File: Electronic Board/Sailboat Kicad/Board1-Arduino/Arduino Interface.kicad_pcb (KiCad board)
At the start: 2 copper layers, 68.6 x 99.7 mm, 60 parts, among them J1 Conn_01x02, J10 Conn_01x02, J11 Conn_01x03_Male, J12 Conn_01x03_Male, J13 Conn_01x03_Male, J14 Conn_01x03_Male, J15 Conn_01x04, J16 Conn_01x04, J17 Conn_01x04, J18 Conn_01x04, J19 Conn_01x03, J2 Conn_01x08, J20 Conn_01x03, J21 Conn_01x02, J22 Conn_01x02, J23 Conn_01x06, J24 Conn_01x03, J25 Conn_01x06, J26 Conn_02x02_Odd_Even, J27 Conn_01x08, J3 Conn_01x08, J31 Conn_01x04, J32 Conn_01x04, J34 Conn_01x02, J35 Conn_01x02, J36 Conn_01x02, J37 Conn_01x02, J4 Conn_01x08, J5 Conn_02x18_Odd_Even, J6 Conn_01x08, J7 Conn_01x08, J8 Conn_01x08, J9 Conn_01x02, U1 L7805, U2 L7805, U3 L7805

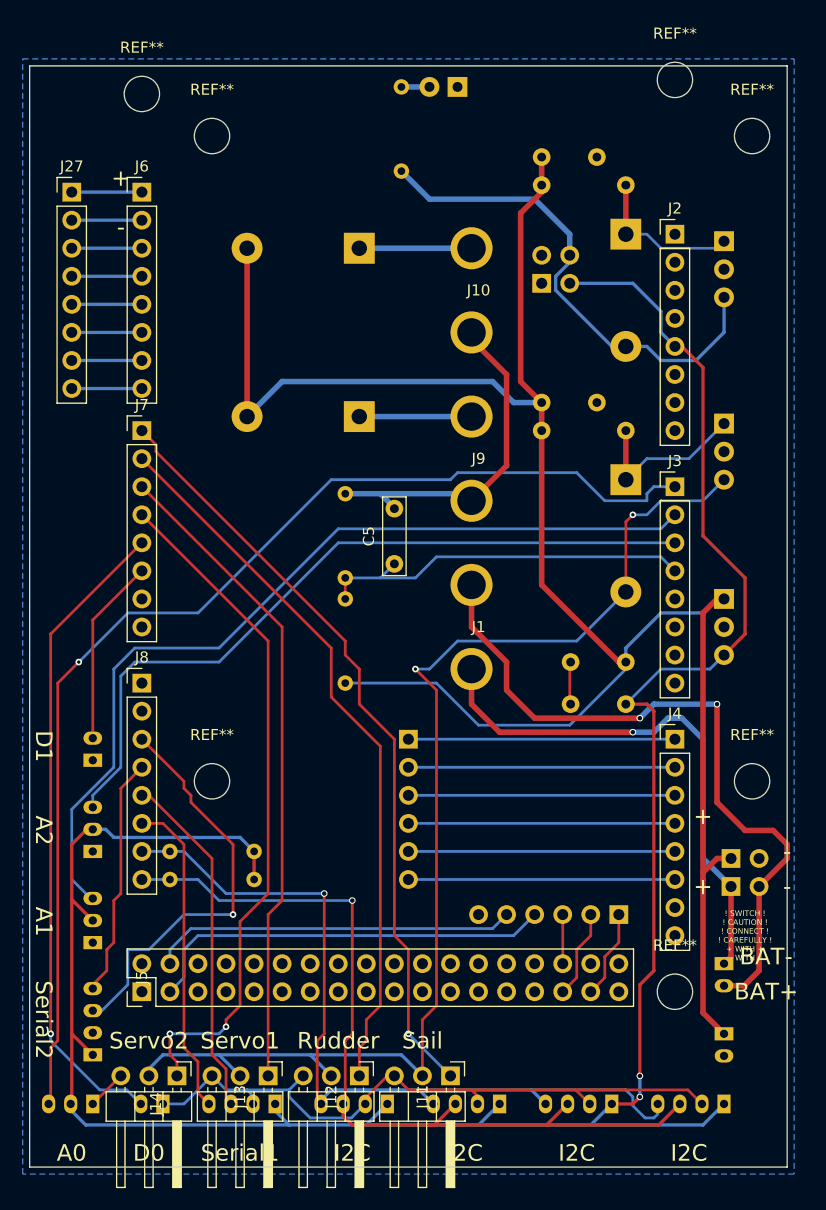
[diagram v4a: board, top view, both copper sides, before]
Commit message: Updated version of Kicad, rendered images and BOM
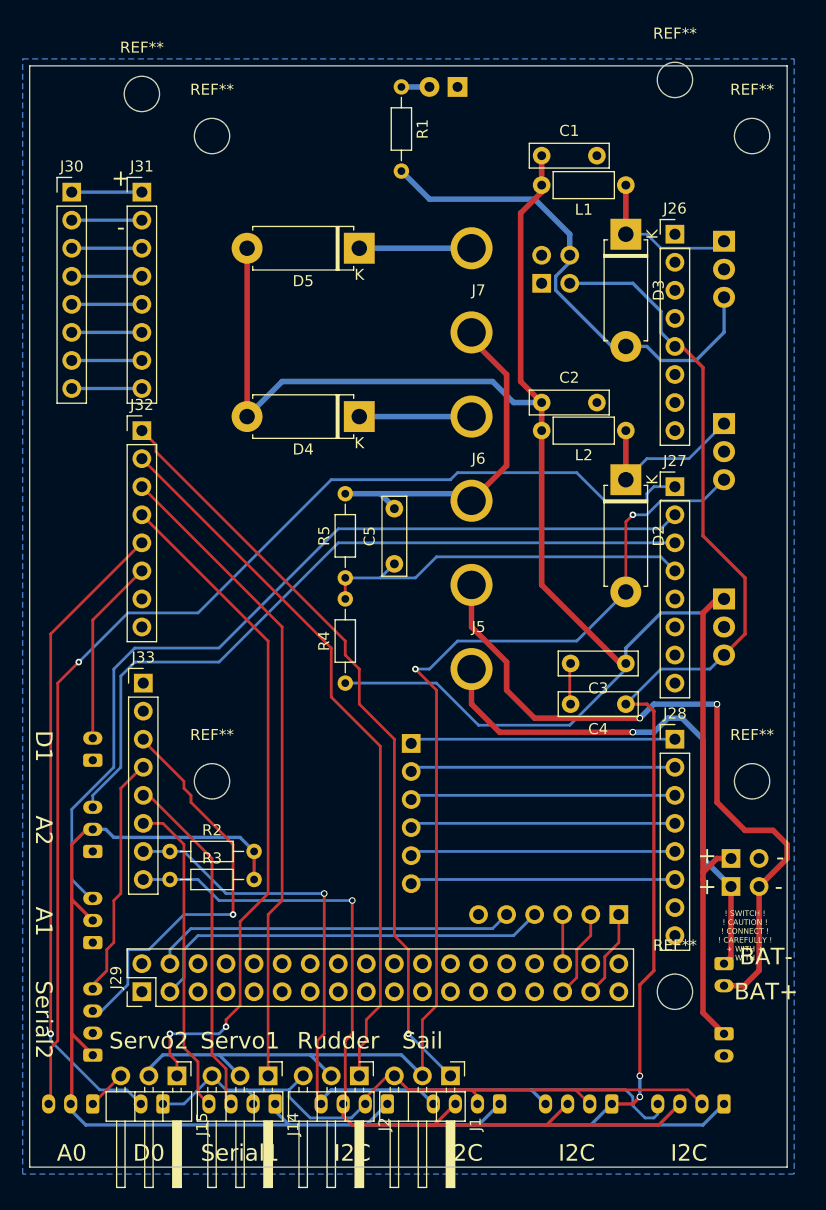
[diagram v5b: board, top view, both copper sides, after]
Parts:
- removed J34, J35: Conn_01x02, Connectors_JST:JST_PH_S2B-PH-K_02x2.00mm_Angled
- removed J36, J37: Conn_01x02, Pin_Headers:Pin_Header_Straight_1x02_Pitch2.54mm
- added J28: Conn_01x08_Male, Connector_PinHeader_2.54mm:PinHeader_1x08_P2.54mm_Vertical, F.Cu at (177.2, 114.3)
- added J29: Conn_02x18_Odd_Even, Connector_PinHeader_2.54mm:PinHeader_2x18_P2.54mm_Vertical, F.Cu at (128.9, 137.2)
- added J30: Conn_01x08_Male, Connector_PinHeader_2.54mm:PinHeader_1x08_P2.54mm_Vertical, F.Cu at (122.6, 64.8)
- added J33: Conn_01x08_Male, Connector_PinHeader_2.54mm:PinHeader_1x08_P2.54mm_Vertical, F.Cu at (129.0, 109.2)
- C1, C2: footprint Capacitors_THT:C_Rect_L7.0mm_W2.0mm_P5.00mm -> Capacitor_THT:C_Rect_L7.0mm_W2.0mm_P5.00mm; moved to F.Cu
- C3, C4: footprint Capacitors_THT:C_Rect_L7.0mm_W3.5mm_P5.00mm -> Capacitor_THT:C_Rect_L7.0mm_W2.0mm_P5.00mm; moved to F.Cu
- C5: footprint Capacitors_THT:C_Rect_L7.0mm_W2.0mm_P5.00mm -> Capacitor_THT:C_Rect_L7.0mm_W2.0mm_P5.00mm
- D2, D3, D4, D5: footprint Diodes_THT:D_5W_P10.16mm_Horizontal -> Diode_THT:D_5W_P10.16mm_Horizontal; moved to F.Cu
- J1: value Conn_01x02 -> Conn_01x03_Male; footprint Sailboat:BAT-CONN -> Connector_PinHeader_2.54mm:PinHeader_1x03_P2.54mm_Horizontal
- J10: value Conn_01x02 -> Conn_01x02_Male; footprint Sailboat:BAT-CONN -> Connector_JST:JST_PH_S2B-PH-K_1x02_P2.00mm_Horizontal; moved to B.Cu
- J11: value Conn_01x03_Male -> Conn_01x02_Male; footprint Pin_Headers:Pin_Header_Angled_1x03_Pitch2.54mm -> Connector_PinHeader_2.54mm:PinHeader_1x02_P2.54mm_Vertical; moved to B.Cu
- J12, J13: value Conn_01x03_Male -> Conn_01x04_Male; footprint Pin_Headers:Pin_Header_Angled_1x03_Pitch2.54mm -> Connector_JST:JST_PH_S4B-PH-K_1x04_P2.00mm_Horizontal; moved to B.Cu
- J14: footprint Pin_Headers:Pin_Header_Angled_1x03_Pitch2.54mm -> Connector_PinHeader_2.54mm:PinHeader_1x03_P2.54mm_Horizontal
- J15: value Conn_01x04 -> Conn_01x03_Male; footprint Connectors_JST:JST_PH_S4B-PH-K_04x2.00mm_Angled -> Connector_PinHeader_2.54mm:PinHeader_1x03_P2.54mm_Horizontal; moved to F.Cu
- J16, J17: value Conn_01x04 -> Conn_01x06_Male; footprint Connectors_JST:JST_PH_S4B-PH-K_04x2.00mm_Angled -> Connector_PinHeader_2.54mm:PinHeader_1x06_P2.54mm_Vertical
- J18: value Conn_01x04 -> Conn_01x03_Male; footprint Connectors_JST:JST_PH_S4B-PH-K_04x2.00mm_Angled -> Connector_JST:JST_PH_S3B-PH-K_1x03_P2.00mm_Horizontal
- J19: value Conn_01x03 -> Conn_01x03_Male; footprint Connectors_JST:JST_PH_S3B-PH-K_03x2.00mm_Angled -> Connector_JST:JST_PH_S3B-PH-K_1x03_P2.00mm_Horizontal
- J2: value Conn_01x08 -> Conn_01x03_Male; footprint Pin_Headers:Pin_Header_Straight_1x08_Pitch2.54mm -> Connector_PinHeader_2.54mm:PinHeader_1x03_P2.54mm_Horizontal
- J20: value Conn_01x03 -> Conn_01x02_Male; footprint Connectors_JST:JST_PH_S3B-PH-K_03x2.00mm_Angled -> Connector_JST:JST_PH_S2B-PH-K_1x02_P2.00mm_Horizontal
- J21: value Conn_01x02 -> Conn_01x02_Male; footprint Connectors_JST:JST_PH_S2B-PH-K_02x2.00mm_Angled -> Connector_JST:JST_PH_S2B-PH-K_1x02_P2.00mm_Horizontal
- J22: value Conn_01x02 -> Conn_01x03_Male; footprint Connectors_JST:JST_PH_S2B-PH-K_02x2.00mm_Angled -> Connector_JST:JST_PH_S3B-PH-K_1x03_P2.00mm_Horizontal
- J23, J25: value Conn_01x06 -> Conn_01x04_Male; footprint Pin_Headers:Pin_Header_Straight_1x06_Pitch2.54mm -> Connector_JST:JST_PH_S4B-PH-K_1x04_P2.00mm_Horizontal
- J24: value Conn_01x03 -> Conn_02x02_Odd_Even; footprint Connectors_JST:JST_PH_S3B-PH-K_03x2.00mm_Angled -> Connector_PinHeader_2.54mm:PinHeader_2x02_P2.54mm_Vertical
- J26: value Conn_02x02_Odd_Even -> Conn_01x08_Male; footprint Pin_Headers:Pin_Header_Straight_2x02_Pitch2.54mm -> Connector_PinHeader_2.54mm:PinHeader_1x08_P2.54mm_Vertical; moved to F.Cu
- J27: value Conn_01x08 -> Conn_01x08_Male; footprint Pin_Headers:Pin_Header_Straight_1x08_Pitch2.54mm -> Connector_PinHeader_2.54mm:PinHeader_1x08_P2.54mm_Vertical
- J3, J4: value Conn_01x08 -> Conn_01x04_Male; footprint Pin_Headers:Pin_Header_Straight_1x08_Pitch2.54mm -> Connector_JST:JST_PH_S4B-PH-K_1x04_P2.00mm_Horizontal; moved to B.Cu
- J31, J32: value Conn_01x04 -> Conn_01x08_Male; footprint Connectors_JST:JST_PH_S4B-PH-K_04x2.00mm_Angled -> Connector_PinHeader_2.54mm:PinHeader_1x08_P2.54mm_Vertical; moved to F.Cu
- J5: value Conn_02x18_Odd_Even -> Conn_01x02_Female; footprint Pin_Headers:Pin_Header_Straight_2x18_Pitch2.54mm -> Sailboat:BAT-CONN
- J6, J7: value Conn_01x08 -> Conn_01x02_Female; footprint Pin_Headers:Pin_Header_Straight_1x08_Pitch2.54mm -> Sailboat:BAT-CONN
- J8: value Conn_01x08 -> Conn_01x02_Male; footprint Pin_Headers:Pin_Header_Straight_1x08_Pitch2.54mm -> Connector_JST:JST_PH_S2B-PH-K_1x02_P2.00mm_Horizontal; moved to B.Cu
- J9: value Conn_01x02 -> Conn_01x02_Male; footprint Sailboat:BAT-CONN -> Connector_PinHeader_2.54mm:PinHeader_1x02_P2.54mm_Vertical; moved to B.Cu
- L1, L2: footprint Inductors_THT:L_Axial_L5.3mm_D2.2mm_P7.62mm_Horizontal_Vishay_IM-1 -> Inductor_THT:L_Axial_L5.3mm_D2.2mm_P7.62mm_Horizontal_Vishay_IM-1; moved to F.Cu
- R1, R2, R3, R4, R5: footprint Resistors_THT:R_Axial_DIN0204_L3.6mm_D1.6mm_P7.62mm_Horizontal -> Resistor_THT:R_Axial_DIN0204_L3.6mm_D1.6mm_P7.62mm_Horizontal; moved to F.Cu
- U1, U2, U3: footprint TO_SOT_Packages_THT:TO-220-3_Vertical -> Package_TO_SOT_THT:TO-220-3_Vertical
- moved J31 83.4 mm to (128.9, 64.8), turned to 0 degrees
- moved J2 81.4 mm to (148.6, 144.8), turned to 270 degrees
- moved J10 71.1 mm to (181.6, 141.0), turned to 270 degrees
- moved J24 65.6 mm to (165.1, 73.0), turned to 0 degrees
- moved J27 60.8 mm to (177.2, 91.4)
- moved J8 58.5 mm to (181.6, 134.6), turned to 270 degrees
- moved J3 58.1 mm to (161.3, 147.3), turned to 180 degrees
- moved J32 56.7 mm to (128.9, 86.4), turned to 0 degrees
- moved J25 49.3 mm to (124.5, 142.9)
- moved J9 45.3 mm to (182.2, 127.6), turned to 270 degrees
- moved J5 44.5 mm to (158.8, 104.1), turned to 180 degrees
- moved J4 42.0 mm to (151.1, 147.3), turned to 180 degrees
- moved J1 40.7 mm to (156.8, 144.8), turned to 270 degrees
- moved J6 38.4 mm to (158.8, 88.9), turned to 180 degrees
- moved J16 37.4 mm to (153.3, 114.7)
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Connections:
- J1 pad 1: Net-(J1-Pad1) -> Sail
- J1 pad 2: Net-(J1-Pad2) -> /Connectors/5V-Servo
- J10 pad 1: GND -> BAT+
- J10 pad 2: Net-(D5-Pad1) -> GND
- J11 pad 1: Sail -> BAT+
- J11 pad 2: /Connectors/5V-Servo -> GND
- J12 pad 1: Rudder -> /ArduinoMega/5V
- J12 pad 2: /Connectors/5V-Servo -> GND
- J12 pad 3: GND -> SCL
- J13 pad 1: Servo1 -> /ArduinoMega/5V
- J13 pad 2: /Connectors/5V-Servo -> GND
- J13 pad 3: GND -> SCL
- J14 pad 1: Servo2 -> Servo1
- J15 pad 1: /ArduinoMega/5V -> Servo2
- J15 pad 2: GND -> /Connectors/5V-Servo
- J15 pad 3: SCL -> GND
- J16 pad 1: /ArduinoMega/5V -> RC1
- J16 pad 2: GND -> RC2
- J16 pad 3: SCL -> RC3
- J16 pad 4: SDA -> RC4
- J17 pad 1: /ArduinoMega/5V -> SCK
- J17 pad 2: GND -> MISO
- J17 pad 3: SCL -> MOSI
- J17 pad 4: SDA -> CD
- J18 pad 1: /ArduinoMega/5V -> GND
- J18 pad 2: GND -> /ArduinoMega/5V
- J18 pad 3: SCL -> A0
- J19 pad 3: A0 -> A1
- J2 pad 1: Net-(J2-Pad1) -> Rudder
- J2 pad 2: Net-(J2-Pad2) -> /Connectors/5V-Servo
- J2 pad 3: /ArduinoMega/RESET -> GND
- J20 pad 2: /ArduinoMega/5V -> D0
- J21 pad 2: D0 -> D1
- J22 pad 2: D1 -> /ArduinoMega/5V
- J23 pad 1: RC1 -> /ArduinoMega/5V
- J23 pad 2: RC2 -> GND
- J23 pad 3: RC3 -> TX_1
- J23 pad 4: RC4 -> RX_1
- J24 pad 3: A2 -> GND
- J25 pad 1: SCK -> /ArduinoMega/5V
- J25 pad 2: MISO -> GND
- J25 pad 3: MOSI -> TX_2
- J25 pad 4: CD -> RX_2
- J26 pad 1: GND -> Net-(J26-Pad1)
- J26 pad 2: /ArduinoMega/5V -> Net-(J26-Pad2)
- J26 pad 3: GND -> /ArduinoMega/RESET
- J26 pad 4: /Connectors/5V-Rpi -> /ArduinoMega/3.3V
- J27 pad 1: /ArduinoMega/AREF -> A0
- J27 pad 2: GND -> A1
- J27 pad 3: /ArduinoMega/13 -> A2
- J27 pad 4: /ArduinoMega/12 -> /ArduinoMega/A3
- J27 pad 5: /ArduinoMega/11 -> /ArduinoMega/A4
- J27 pad 6: /ArduinoMega/10 -> /ArduinoMega/A5
- J27 pad 7: /ArduinoMega/9 -> /ArduinoMega/A6
- J27 pad 8: /ArduinoMega/8 -> /ArduinoMega/A7
- J3 pad 1: A0 -> /ArduinoMega/5V
- J3 pad 2: A1 -> GND
- J3 pad 3: A2 -> SCL
- J3 pad 4: /ArduinoMega/A3 -> SDA
- J31 pad 1: /ArduinoMega/5V -> /ArduinoMega/AREF
- J31 pad 3: TX_1 -> /ArduinoMega/13
- J31 pad 4: RX_1 -> /ArduinoMega/12
- J32 pad 1: /ArduinoMega/5V -> Sail
- J32 pad 2: GND -> Rudder
- J32 pad 3: TX_2 -> Servo1
- J32 pad 4: RX_2 -> Servo2
- J4 pad 1: RC1 -> /ArduinoMega/5V
- J4 pad 2: RC2 -> GND
- J4 pad 3: RC3 -> SCL
- J4 pad 4: RC4 -> SDA
- J6 pad 1: /ArduinoMega/AREF -> GND
- J6 pad 2: GND -> Net-(D4-Pad1)
- J7 pad 1: Sail -> GND
- J7 pad 2: Rudder -> Net-(D5-Pad1)
- J8 pad 1: /ArduinoMega/14-TX3 -> Net-(J5-Pad1)
- J8 pad 2: /ArduinoMega/15-RX3 -> Net-(J5-Pad2)
- J9 pad 1: GND -> Net-(J5-Pad1)
- J9 pad 2: Net-(D4-Pad1) -> Net-(J5-Pad2)
- U1 pad 1: Net-(D3-Pad1) -> Net-(D2-Pad1)
- U1 pad 3: /Connectors/5V-Rpi -> /Connectors/5V-Servo
- U2 pad 1: Net-(D2-Pad1) -> Net-(D3-Pad1)
- U2 pad 3: /Connectors/5V-Servo -> /Connectors/5V-Rpi
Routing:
- net Net-(J5-Pad2): track 0.00 -> 64.5 mm, vias 0 -> 2
- net Net-(J1-Pad2): track 64.5 -> 0.00 mm, vias 2 -> 0
- net Net-(J5-Pad1): track 0.00 -> 48.1 mm, vias 0 -> 1
- net Net-(J1-Pad1): track 48.1 -> 0.00 mm, vias 1 -> 0
